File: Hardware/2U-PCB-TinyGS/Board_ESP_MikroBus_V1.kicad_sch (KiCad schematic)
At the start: 15 parts, among them J1 Bus Standard, J1 Conn_01x19, J2 Conn_01x19, U1 ESP32-DEVKITC-32D

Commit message: Design changed
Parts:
- added I2C2, I2C3, I2C4, I2C5: Grove, Connector:NS-Tech_Grove_1x04_P2mm_Vertical, symbol Connector_Generic:Conn_01x04
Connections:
- net +3.3V: now also I2C2.3 (Pin_3), I2C3.3 (Pin_3), I2C4.3 (Pin_3), I2C5.3 (Pin_3)
- net GNDREF: now also I2C2.4 (Pin_4), I2C3.4 (Pin_4), I2C4.4 (Pin_4), I2C5.4 (Pin_4)
- net I2C_SCL: now also I2C2.1 (Pin_1), I2C3.1 (Pin_1), I2C4.1 (Pin_1), I2C5.1 (Pin_1)
- net I2C_SDA: now also I2C2.2 (Pin_2), I2C3.2 (Pin_2), I2C4.2 (Pin_2), I2C5.2 (Pin_2)
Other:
- moved on the sheet: 3.3, 5V1, C1, C2, IO_32/33

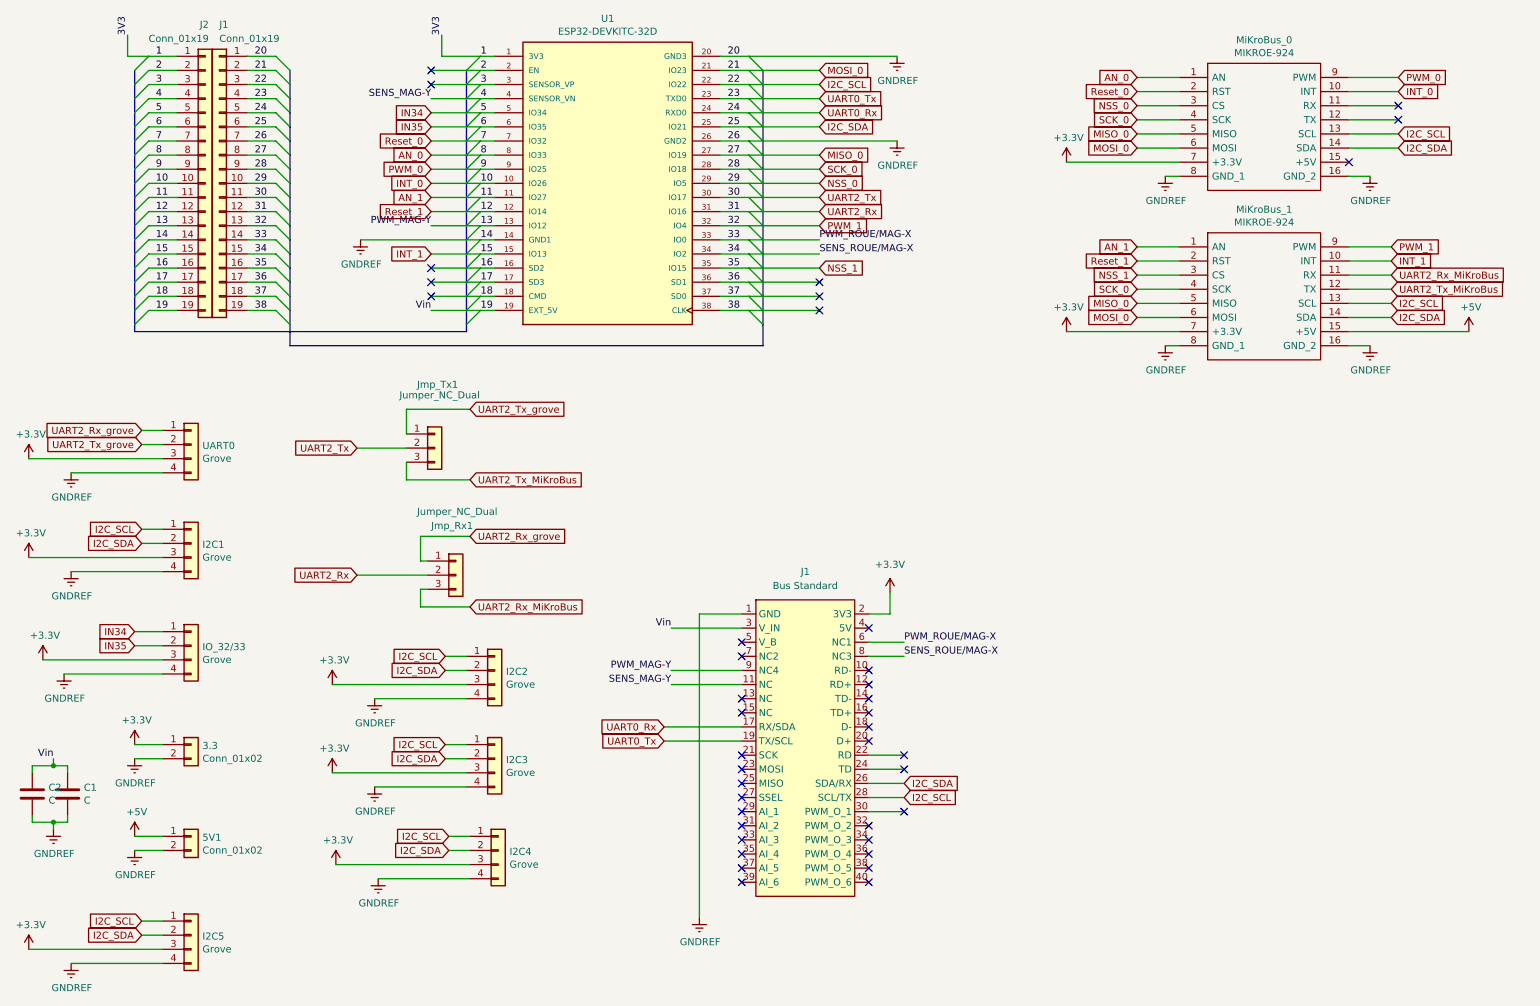
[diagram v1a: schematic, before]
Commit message: Selection CAN juper added. Can buffer added
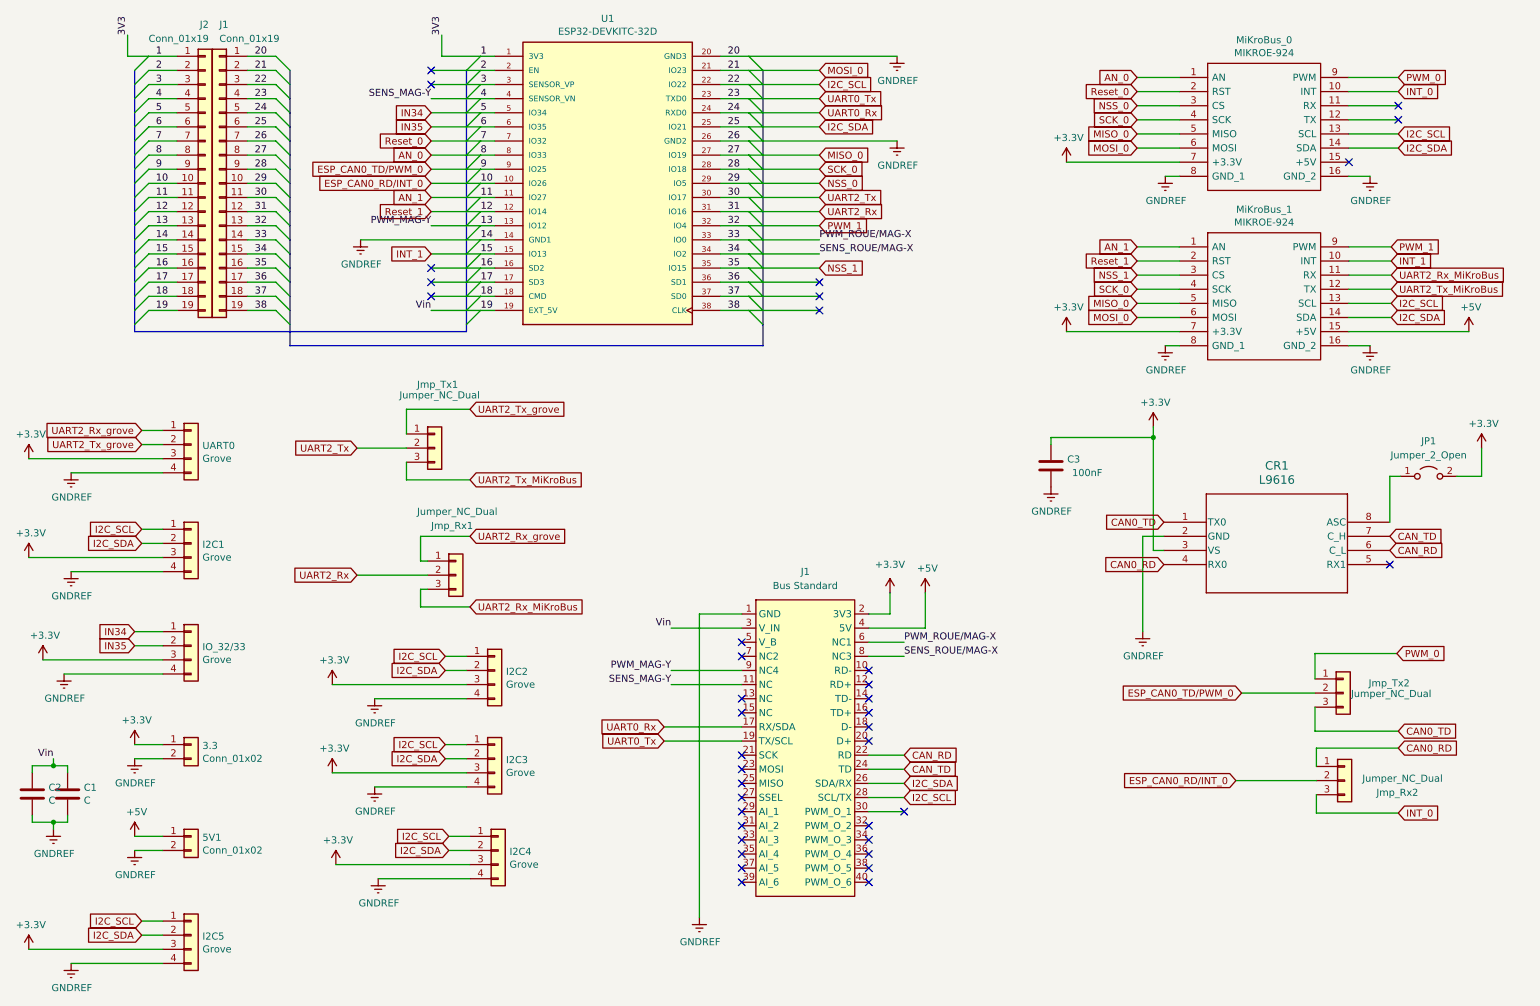
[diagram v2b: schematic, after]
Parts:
- added C3: 100nF, Capacitor_SMD:C_0805_2012Metric_Pad1.18x1.45mm_HandSolder, symbol Device:C
- added CR1: L9616, CAN_buffer:SO-8_STM, symbol CAN_buffer:L9616
- added JP1: Jumper_2_Open, Connector_PinHeader_2.54mm:PinHeader_1x02_P2.54mm_Vertical, symbol Jumper:Jumper_2_Open
- added Jmp_Rx2, Jmp_Tx2: Jumper_NC_Dual, Connector_PinHeader_2.54mm:PinHeader_1x03_P2.54mm_Vertical, symbol Connector_Generic:Conn_01x03
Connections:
- net +3.3V: now also C3.1, CR1.3 (VS), JP1.2 (B)
- net +5V: now also J1.4 (5V)
- net GNDREF: now also C3.2, CR1.2 (GND)
- net INT_0: now also Jmp_Rx2.3 (Pin_3); no longer J1.10 (Pin_10), U1.10 (IO26)
- net PWM_0: now also Jmp_Tx2.1 (Pin_1); no longer J1.9 (Pin_9), U1.9 (IO25)
- net CAN_RD: now reaches J1.22 (RD)
- net CAN_RD: now also CR1.6 (C_L)
- net CAN_TD: now reaches J1.24 (TD)
- net CAN_TD: now also CR1.7 (C_H)
- new net: CR1.8 (ASC), JP1.1 (A)
- new net CAN0_RD: CR1.4 (RX0), Jmp_Rx2.1 (Pin_1)
- new net CAN0_TD: CR1.1 (TX0), Jmp_Tx2.3 (Pin_3)
- new net ESP_CAN0_RD/INT_0: J1.10 (Pin_10), Jmp_Rx2.2 (Pin_2), U1.10 (IO26)
- new net ESP_CAN0_TD/PWM_0: J1.9 (Pin_9), Jmp_Tx2.2 (Pin_2), U1.9 (IO25)
- no-connect marks 40 -> 38
